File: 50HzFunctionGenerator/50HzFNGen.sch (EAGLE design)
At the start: 23 parts, among them IC2 7812L, IC4 TL082P, X2 MAB32

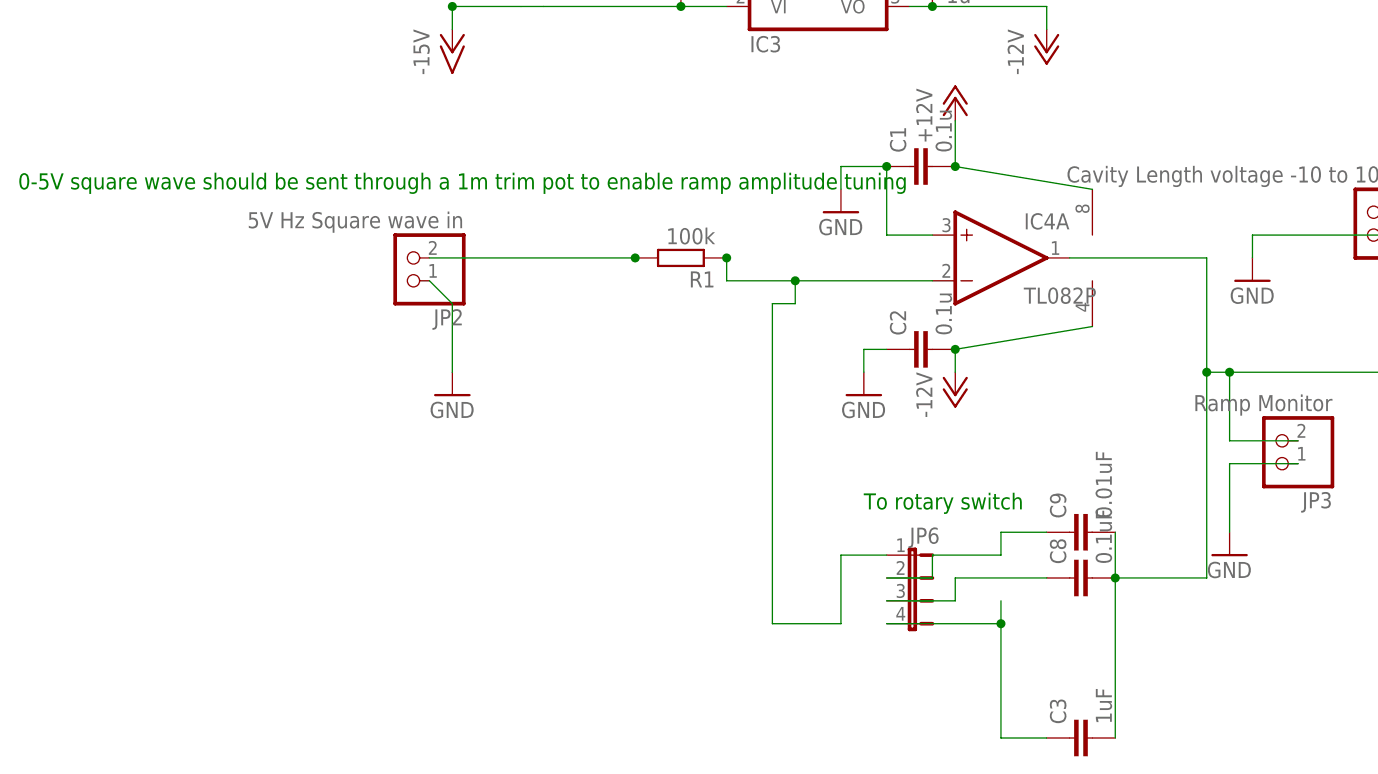
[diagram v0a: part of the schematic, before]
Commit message: Some changes to make the function generator board work
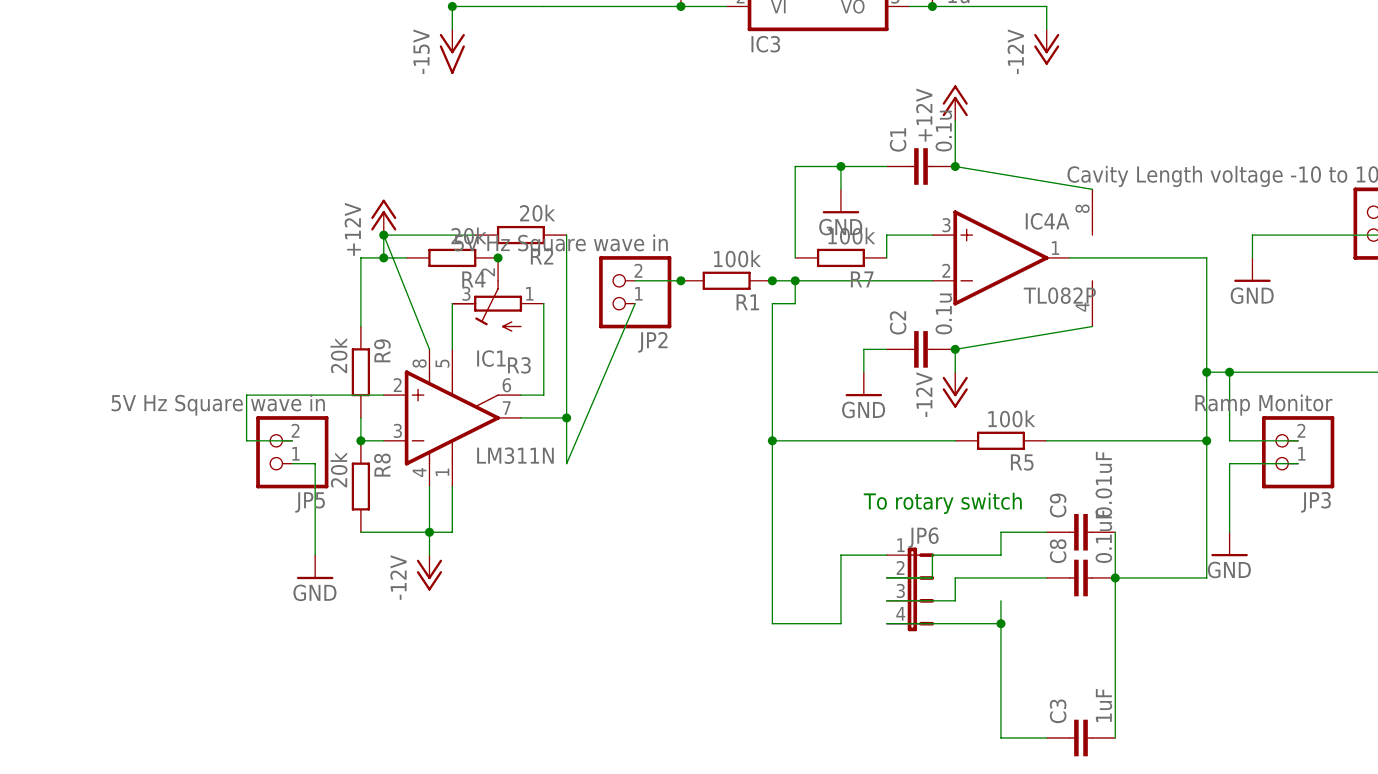
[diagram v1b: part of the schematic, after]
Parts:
- added IC1: LM311N, linear:LM311N
- added JP5: 5V Hz Square wave in, pinhead:PINHD-1X2
- added R2, R4, R8, R9: 20k, resistor:R-EU_0207/10
- added R3: (no value), resistor:R-TRIMM64P
- added R5, R7: 100k, resistor:R-EU_0207/10
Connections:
- new net N$12: IC1.OUT, JP2.1, R2.1
- new net N$16: IC1.ON, R3.A
- new net N$18: IC1.ON/STR, R3.E
- new net N$19: R3.S, R4.1
- new net N$20: IC4A.+IN, R7.1
- new net N$23: IC1.+IN, JP5.2
- new net N$25: IC1.-IN, R8.1, R9.2
- net +12V: now also IC1.V+, R2.2, R4.2, R9.1
- net -12V: now also IC1.GND, IC1.V-, R8.2
- net GND: now also JP5.1, R7.2; no longer IC4A.+IN, JP2.1
- net N$14: now also R5.1
- net N$17: now also R5.2
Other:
- note removed: "0-5V square wave should be sent through a 1m trim pot to enable ramp amplitude tuning"
- moved on the sheet: JP2, R1

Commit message: finished version of the board
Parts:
- removed JP5: 5V Hz Square wave in, pinhead:PINHD-1X2
- added JP7: (no value), jumper:JP2E
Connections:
- net GND: now also JP7.3, X2.11, X2.12, X2.14, X2.15, X2.16; no longer JP5.1
- net N$12: now also JP7.2; no longer JP2.1
- net N$23: now also JP7.1; no longer JP5.2
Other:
- moved on the sheet: C3
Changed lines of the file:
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@@
 <?xml version="1.0" encoding="utf-8"?>
 <!DOCTYPE eagle SYSTEM "eagle.dtd">
-<eagle version="6.4">
+<eagle version="6.5.0">
 <drawing>
 <settings>
@@
 <part name="R5" library="resistor" deviceset="R-EU_" device="0207/10" value="100k"/>
 <part name="R7" library="resistor" deviceset="R-EU_" device="0207/10" value="100k"/>
-<part name="JP5" library="pinhead" deviceset="PINHD-1X2" device="" value="5V Hz Square wave in "/>
-<part name="GND6" library="supply1" deviceset="GND" device=""/>
 <part name="R8" library="resistor" deviceset="R-EU_" device="0207/10" value="20k"/>
 <part name="R9" library="resistor" deviceset="R-EU_" device="0207/10" value="20k"/>
+<part name="JP7" library="jumper" deviceset="JP2E" device=""/>
+<part name="GND6" library="supply1" deviceset="GND" device=""/>
 </parts>
 <sheets>
@@
 <instance part="JP2" gate="G$1" x="35.56" y="55.88" rot="R180"/>
 <instance part="R1" gate="G$1" x="48.26" y="55.88" rot="R180"/>
-<instance part="C3" gate="G$1" x="86.36" y="5.08" rot="R90"/>
+<instance part="C3" gate="G$1" x="86.36" y="17.78" rot="R90"/>
 <instance part="C8" gate="G$1" x="86.36" y="22.86" rot="R90"/>
 <instance part="C9" gate="G$1" x="86.36" y="27.94" rot="R90"/>
@@
 <instance part="R5" gate="G$1" x="78.74" y="38.1" rot="R180"/>
 <instance part="R7" gate="G$1" x="60.96" y="58.42" rot="R180"/>
-<instance part="JP5" gate="G$1" x="-2.54" y="38.1" rot="R180"/>
-<instance part="GND6" gate="1" x="2.54" y="22.86"/>
 <instance part="R8" gate="G$1" x="7.62" y="33.02" rot="R270"/>
 <instance part="R9" gate="G$1" x="7.62" y="45.72" rot="R270"/>
+<instance part="JP7" gate="1" x="-2.54" y="35.56" rot="R270"/>
+<instance part="GND6" gate="1" x="0" y="25.4"/>
 </instances>
 <busses>
@@
 <pinref part="SUPPLY1" gate="GND" pin="GND"/>
 <pinref part="X2" gate="G$1" pin="1"/>
+<pinref part="X2" gate="G$1" pin="11"/>
+<pinref part="X2" gate="G$1" pin="16"/>
+<wire x1="180.34" y1="101.6" x2="182.88" y2="101.6" width="0.1524" layer="91"/>
+<wire x1="182.88" y1="101.6" x2="185.42" y2="101.6" width="0.1524" layer="91"/>
+<wire x1="185.42" y1="101.6" x2="187.96" y2="101.6" width="0.1524" layer="91"/>
+<wire x1="187.96" y1="101.6" x2="190.5" y2="101.6" width="0.1524" layer="91"/>
+<wire x1="190.5" y1="101.6" x2="193.04" y2="101.6" width="0.1524" layer="91"/>
+<wire x1="185.42" y1="101.6" x2="185.42" y2="83.82" width="0.1524" layer="91"/>
+<junction x="185.42" y="101.6"/>
+<wire x1="185.42" y1="83.82" x2="162.56" y2="81.28" width="0.1524" layer="91"/>
+<wire x1="162.56" y1="81.28" x2="162.56" y2="96.52" width="0.1524" layer="91"/>
+<wire x1="162.56" y1="96.52" x2="154.94" y2="96.52" width="0.1524" layer="91"/>
+<junction x="154.94" y="96.52"/>
+<pinref part="X2" gate="G$1" pin="12"/>
+<junction x="182.88" y="101.6"/>
+<junction x="180.34" y="101.6"/>
+<pinref part="X2" gate="G$1" pin="14"/>
+<junction x="187.96" y="101.6"/>
+<pinref part="X2" gate="G$1" pin="15"/>
+<junction x="190.5" y="101.6"/>
+<junction x="193.04" y="101.6"/>
 </segment>
 <segment>
@@
 <wire x1="106.68" y1="60.96" x2="106.68" y2="58.42" width="0.1524" layer="91"/>
 <pinref part="GND2" gate="1" pin="GND"/>
+<wire x1="106.68" y1="60.96" x2="106.68" y2="58.42" width="0.1524" layer="91"/>
+<junction x="106.68" y="58.42"/>
+<junction x="106.68" y="60.96"/>
 </segment>
 <segment>
@@
 </segment>
 <segment>
-<pinref part="JP5" gate="G$1" pin="1"/>
-<wire x1="0" y1="35.56" x2="2.54" y2="35.56" width="0.1524" layer="91"/>
-<wire x1="2.54" y1="35.56" x2="2.54" y2="25.4" width="0.1524" layer="91"/>
+<pinref part="JP7" gate="1" pin="3"/>
+<wire x1="-5.08" y1="33.02" x2="-5.08" y2="27.94" width="0.1524" layer="91"/>
 <pinref part="GND6" gate="1" pin="GND"/>
+<wire x1="-5.08" y1="27.94" x2="0" y2="27.94" width="0.1524" layer="91"/>
 </segment>
 </net>
@@
 <pinref part="IC4" gate="A" pin="-IN"/>
 <wire x1="53.34" y1="53.34" x2="55.88" y2="53.34" width="0.1524" layer="91"/>
-<wire x1="53.34" y1="17.78" x2="53.34" y2="38.1" width="0.1524" layer="91"/>
+<wire x1="53.34" y1="25.4" x2="53.34" y2="38.1" width="0.1524" layer="91"/>
 <pinref part="R1" gate="G$1" pin="1"/>
 <wire x1="53.34" y1="38.1" x2="53.34" y2="53.34" width="0.1524" layer="91"/>
@@
 <junction x="55.88" y="55.88"/>
 <junction x="53.34" y="55.88"/>
-<wire x1="53.34" y1="17.78" x2="60.96" y2="17.78" width="0.1524" layer="91"/>
-<wire x1="60.96" y1="17.78" x2="60.96" y2="25.4" width="0.1524" layer="91"/>
+<wire x1="53.34" y1="25.4" x2="66.04" y2="25.4" width="0.1524" layer="91"/>
 <pinref part="JP6" gate="G$1" pin="1"/>
-<wire x1="60.96" y1="25.4" x2="66.04" y2="25.4" width="0.1524" layer="91"/>
 <pinref part="R5" gate="G$1" pin="2"/>
 <wire x1="73.66" y1="38.1" x2="53.34" y2="38.1" width="0.1524" layer="91"/>
@@
 <junction x="78.74" y="17.78"/>
 <pinref part="C3" gate="G$1" pin="1"/>
-<wire x1="83.82" y1="5.08" x2="78.74" y2="5.08" width="0.1524" layer="91"/>
-<wire x1="78.74" y1="5.08" x2="78.74" y2="17.78" width="0.1524" layer="91"/>
+<wire x1="83.82" y1="17.78" x2="78.74" y2="17.78" width="0.1524" layer="91"/>
 </segment>
 </net>
@@
 <segment>
 <wire x1="78.74" y1="27.94" x2="78.74" y2="25.4" width="0.1524" layer="91"/>
-<wire x1="78.74" y1="25.4" x2="71.12" y2="25.4" width="0.1524" layer="91"/>
-<wire x1="71.12" y1="25.4" x2="71.12" y2="22.86" width="0.1524" layer="91"/>
+<wire x1="78.74" y1="25.4" x2="76.2" y2="22.86" width="0.1524" layer="91"/>
 <pinref part="JP6" gate="G$1" pin="2"/>
-<wire x1="71.12" y1="22.86" x2="66.04" y2="22.86" width="0.1524" layer="91"/>
+<wire x1="76.2" y1="22.86" x2="66.04" y2="22.86" width="0.1524" layer="91"/>
 <pinref part="C9" gate="G$1" pin="1"/>
 <wire x1="83.82" y1="27.94" x2="78.74" y2="27.94" width="0.1524" layer="91"/>
@@
 <pinref part="C3" gate="G$1" pin="2"/>
 <pinref part="C8" gate="G$1" pin="2"/>
-<wire x1="91.44" y1="5.08" x2="91.44" y2="22.86" width="0.1524" layer="91"/>
+<wire x1="91.44" y1="17.78" x2="91.44" y2="22.86" width="0.1524" layer="91"/>
 <pinref part="C9" gate="G$1" pin="2"/>
 <wire x1="91.44" y1="22.86" x2="91.44" y2="27.94" width="0.1524" layer="91"/>
@@
 <segment>
 <pinref part="C8" gate="G$1" pin="1"/>
-<wire x1="83.82" y1="22.86" x2="73.66" y2="22.86" width="0.1524" layer="91"/>
-<wire x1="73.66" y1="22.86" x2="73.66" y2="20.32" width="0.1524" layer="91"/>
+<wire x1="83.82" y1="22.86" x2="73.66" y2="20.32" width="0.1524" layer="91"/>
 <pinref part="JP6" gate="G$1" pin="3"/>
 <wire x1="73.66" y1="20.32" x2="66.04" y2="20.32" width="0.1524" layer="91"/>
@@
 <pinref part="IC1" gate="A" pin="OUT"/>
 <wire x1="30.48" y1="40.64" x2="25.4" y2="40.64" width="0.1524" layer="91"/>
-<wire x1="30.48" y1="40.64" x2="30.48" y2="35.56" width="0.1524" layer="91"/>
 <junction x="30.48" y="40.64"/>
-<pinref part="JP2" gate="G$1" pin="1"/>
-<wire x1="30.48" y1="35.56" x2="38.1" y2="53.34" width="0.1524" layer="91"/>
+<wire x1="30.48" y1="40.64" x2="30.48" y2="17.78" width="0.1524" layer="91"/>
+<wire x1="30.48" y1="17.78" x2="-5.08" y2="17.78" width="0.1524" layer="91"/>
+<wire x1="-5.08" y1="17.78" x2="-5.08" y2="20.32" width="0.1524" layer="91"/>
+<wire x1="-5.08" y1="20.32" x2="-10.16" y2="35.56" width="0.1524" layer="91"/>
+<pinref part="JP7" gate="1" pin="2"/>
+<wire x1="-10.16" y1="35.56" x2="-5.08" y2="35.56" width="0.1524" layer="91"/>
 </segment>
 </net>
@@
 <wire x1="10.16" y1="43.18" x2="-5.08" y2="43.18" width="0.1524" layer="91"/>
 <wire x1="-5.08" y1="43.18" x2="-5.08" y2="38.1" width="0.1524" layer="91"/>
-<pinref part="JP5" gate="G$1" pin="2"/>
-<wire x1="-5.08" y1="38.1" x2="0" y2="38.1" width="0.1524" layer="91"/>
-</segment>
-</net>
+<pinref part="JP7" gate="1" pin="1"/>
+</segment>
+</net>
